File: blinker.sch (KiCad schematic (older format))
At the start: 28 parts, among them J1 TEST_1P, J2 TEST_1P, J3 TEST_1P, J4 TEST_1P, J5 TEST_1P, J6 TEST_1P, J7 TEST_1P, J8 TEST_1P, J9 TOUCH_PAD_COPPER, Q1 NTR4003NT3G, Q2 NTR4003NT3G, Q3 NTR4003NT3G, Q4 NTR4003NT3G, U1 ASMB-MTB0-0A3A2, U2 ASMB-MTB0-0A3A2, U3 ATTINY85V-10SU

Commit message: decouplign cap and pullup on reset, plus routing almost done
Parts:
- added C1: 100nf, Capacitors_SMD:C_0805_HandSoldering, symbol C
- added R11: 20K, Resistors_SMD:R_0805_HandSoldering, symbol R
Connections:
- wire segments 24 -> 31
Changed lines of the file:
@@
 	8150 5400 7800 5400
 Wire Wire Line
-	3900 3200 4650 3200
+	3900 3200 4600 3200
 Wire Wire Line
-	3800 3300 4650 3300
+	4600 3200 4650 3200
 Wire Wire Line
-	3700 3400 4650 3400
+	3800 3300 4500 3300
 Wire Wire Line
-	3600 3500 4650 3500
+	4500 3300 4650 3300
 Wire Wire Line
-	3500 3600 4650 3600
+	3700 3400 4400 3400
 Wire Wire Line
-	3400 3700 4650 3700
+	4400 3400 4650 3400
+Wire Wire Line
+	3600 3500 4300 3500
+Wire Wire Line
+	4300 3500 4650 3500
+Wire Wire Line
+	3500 3600 4200 3600
+Wire Wire Line
+	4200 3600 4650 3600
+Wire Wire Line
+	3400 3700 4100 3700
+Wire Wire Line
+	4100 3700 4650 3700
 Connection ~ 4600 3200
 Connection ~ 4500 3300
@@
 	0    -1   -1   0
 $EndComp
+$Comp
+L R R11
+U 1 1 59AD0F9D
+P 3250 3700
+F 0 "R11" V 3330 3700 50  0000 C CNN
+F 1 "20K" V 3250 3700 50  0000 C CNN
+F 2 "Resistors_SMD:R_0805_HandSoldering" V 3180 3700 50  0001 C CNN
+F 3 "" H 3250 3700 50  0001 C CNN
+	1    3250 3700
+	0    1    1    0
+$EndComp
+$Comp
+L VCC #PWR016
+U 1 1 59AD13E7
+P 3100 3700
+F 0 "#PWR016" H 3100 3550 50  0001 C CNN
+F 1 "VCC" H 3100 3850 50  0000 C CNN
+F 2 "" H 3100 3700 50  0001 C CNN
+F 3 "" H 3100 3700 50  0001 C CNN
+	1    3100 3700
+	1    0    0    -1
+$EndComp
+$Comp
+L C C1
+U 1 1 59AD17A0
+P 7350 3350
+F 0 "C1" H 7375 3450 50  0000 L CNN
+F 1 "100nf" H 7375 3250 50  0000 L CNN
+F 2 "Capacitors_SMD:C_0805_HandSoldering" H 7388 3200 50  0001 C CNN
+F 3 "" H 7350 3350 50  0001 C CNN
+	1    7350 3350
+	1    0    0    -1
+$EndComp
+Wire Wire Line
+	7350 3500 7350 3700
 $EndSCHEMATC

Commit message: pdc not in sync with sch, but silk almost done
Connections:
- wire segments 31 -> 25
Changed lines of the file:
@@
 	8150 5400 7800 5400
 Wire Wire Line
-	3900 3200 4600 3200
+	3900 3200 4650 3200
 Wire Wire Line
-	4600 3200 4650 3200
+	3800 3300 4650 3300
 Wire Wire Line
-	3800 3300 4500 3300
+	3700 3400 4650 3400
 Wire Wire Line
-	4500 3300 4650 3300
+	3600 3500 4650 3500
 Wire Wire Line
-	3700 3400 4400 3400
+	3500 3600 4650 3600
 Wire Wire Line
-	4400 3400 4650 3400
-Wire Wire Line
-	3600 3500 4300 3500
-Wire Wire Line
-	4300 3500 4650 3500
-Wire Wire Line
-	3500 3600 4200 3600
-Wire Wire Line
-	4200 3600 4650 3600
-Wire Wire Line
-	3400 3700 4100 3700
-Wire Wire Line
-	4100 3700 4650 3700
+	3400 3700 4650 3700
 Connection ~ 4600 3200
 Connection ~ 4500 3300

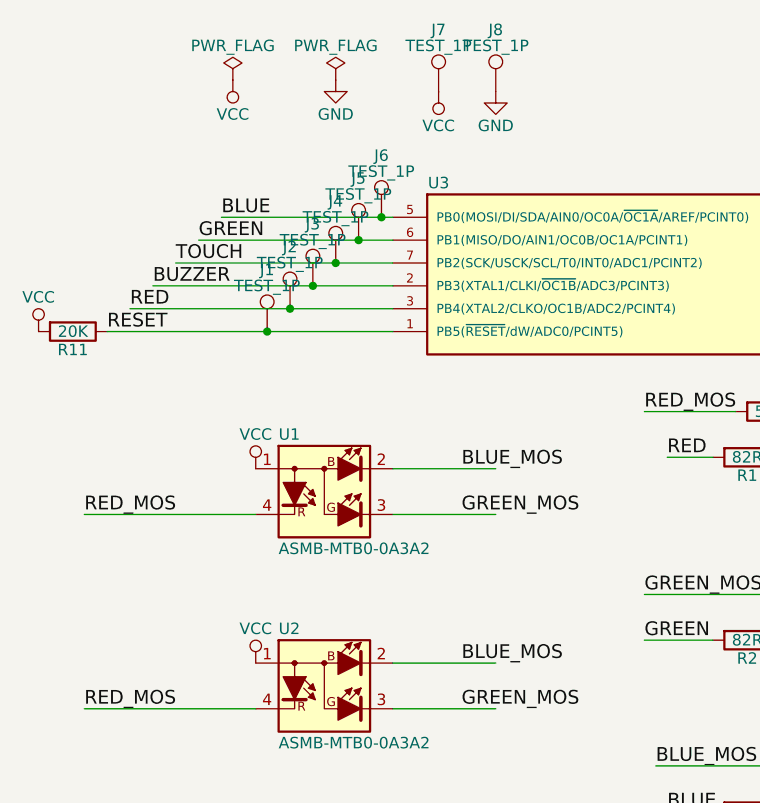
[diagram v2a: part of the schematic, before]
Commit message: assembld board, basic funcs tested. now working on version 0.2
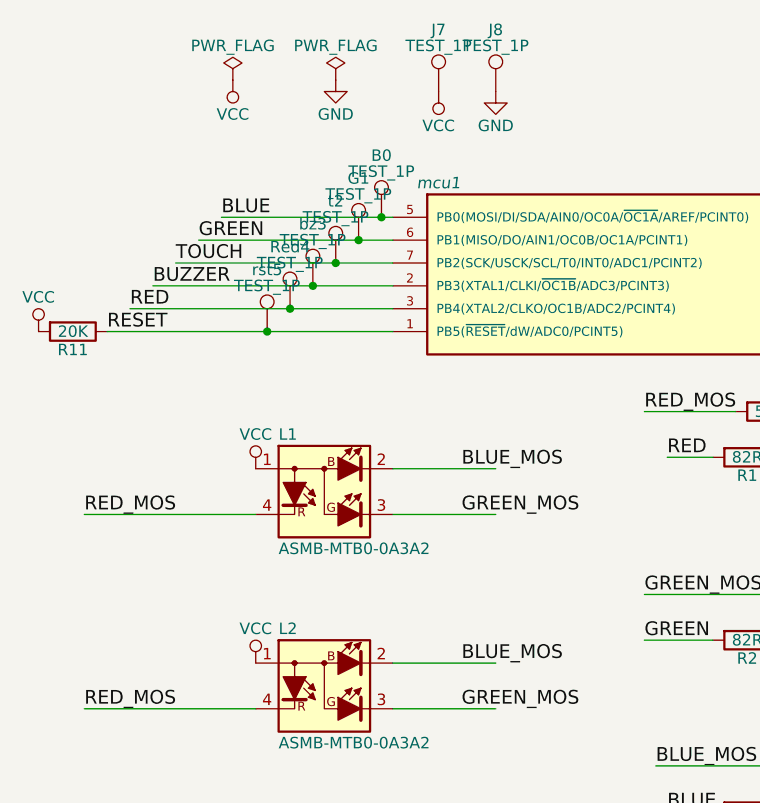
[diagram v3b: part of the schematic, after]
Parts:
- renumbered J6 to B0, J5 to G1, U1 to L1, U2 to L2, J2 to Red4, J3 to bz3, U3 to mcu1, J1 to rst5, J4 to t2
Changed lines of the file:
@@
 $EndDescr
 $Comp
-L ATTINY85-20SU U3
+L ATTINY85-20SU mcu1
 U 1 1 5991F83A
 P 6000 3450
-F 0 "U3" H 4850 3850 50  0000 C CNN
+F 0 "mcu1" H 4850 3850 50  0000 C CIN
 F 1 "ATTINY85V-10SU" H 7000 3050 50  0000 C CNN
 F 2 "Housings_SOIC:SOIC-8_3.9x4.9mm_Pitch1.27mm" H 6950 3450 50  0001 C CIN
@@
 $EndComp
 $Comp
-L ASMB-MTB0-0A3A2 U1
+L ASMB-MTB0-0A3A2 L1
 U 1 1 5993FA5E
 P 4350 4400
-F 0 "U1" H 4150 4650 50  0000 L CNN
+F 0 "L1" H 4150 4650 50  0000 L CNN
 F 1 "ASMB-MTB0-0A3A2" H 4150 4150 50  0000 L CNN
 F 2 "ASMB-MTB0-0A3A2:ASMB-MTB0-0A3A2" H 4720 4410 50  0001 L CNN
@@
 $EndComp
 $Comp
-L ASMB-MTB0-0A3A2 U2
+L ASMB-MTB0-0A3A2 L2
 U 1 1 5993FCE9
 P 4350 5250
-F 0 "U2" H 4150 5500 50  0000 L CNN
+F 0 "L2" H 4150 5500 50  0000 L CNN
 F 1 "ASMB-MTB0-0A3A2" H 4150 5000 50  0000 L CNN
 F 2 "ASMB-MTB0-0A3A2:ASMB-MTB0-0A3A2" H 4720 5260 50  0001 L CNN
@@
 $EndComp
 $Comp
-L TEST_1P J6
+L TEST_1P B0
 U 1 1 59983116
 P 4600 3200
-F 0 "J6" H 4600 3470 50  0000 C CNN
+F 0 "B0" H 4600 3470 50  0000 C CNN
 F 1 "TEST_1P" H 4600 3400 50  0000 C CNN
 F 2 "Wire_Pads:SolderWirePad_single_0-8mmDrill" H 4800 3200 50  0001 C CNN
@@
 $EndComp
 $Comp
-L TEST_1P J5
+L TEST_1P G1
 U 1 1 59983349
 P 4500 3300
-F 0 "J5" H 4500 3570 50  0000 C CNN
+F 0 "G1" H 4500 3570 50  0000 C CNN
 F 1 "TEST_1P" H 4500 3500 50  0000 C CNN
 F 2 "Wire_Pads:SolderWirePad_single_0-8mmDrill" H 4700 3300 50  0001 C CNN
@@
 $EndComp
 $Comp
-L TEST_1P J4
+L TEST_1P t2
 U 1 1 5998339F
 P 4400 3400
-F 0 "J4" H 4400 3670 50  0000 C CNN
+F 0 "t2" H 4400 3670 50  0000 C CNN
 F 1 "TEST_1P" H 4400 3600 50  0000 C CNN
 F 2 "Wire_Pads:SolderWirePad_single_0-8mmDrill" H 4600 3400 50  0001 C CNN
@@
 $EndComp
 $Comp
-L TEST_1P J3
+L TEST_1P bz3
 U 1 1 599833F8
 P 4300 3500
-F 0 "J3" H 4300 3770 50  0000 C CNN
+F 0 "bz3" H 4300 3770 50  0000 C CNN
 F 1 "TEST_1P" H 4300 3700 50  0000 C CNN
 F 2 "Wire_Pads:SolderWirePad_single_0-8mmDrill" H 4500 3500 50  0001 C CNN
@@
 $EndComp
 $Comp
-L TEST_1P J2
+L TEST_1P Red4
 U 1 1 599835BC
 P 4200 3600
-F 0 "J2" H 4200 3870 50  0000 C CNN
+F 0 "Red4" H 4200 3870 50  0000 C CNN
 F 1 "TEST_1P" H 4200 3800 50  0000 C CNN
 F 2 "Wire_Pads:SolderWirePad_single_0-8mmDrill" H 4400 3600 50  0001 C CNN
@@
 $EndComp
 $Comp
-L TEST_1P J1
+L TEST_1P rst5
 U 1 1 5998361B
 P 4100 3700
-F 0 "J1" H 4100 3970 50  0000 C CNN
+F 0 "rst5" H 4100 3970 50  0000 C CNN
 F 1 "TEST_1P" H 4100 3900 50  0000 C CNN
 F 2 "Wire_Pads:SolderWirePad_single_0-8mmDrill" H 4300 3700 50  0001 C CNN

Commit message: 2 version, already built, ready to be tested
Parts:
- added Gnd2, Vcc2: TEST_1P, wrirepad:singlesolderpad, symbol TEST_1P
- B0, G1, Red4, bz3, rst5, t2: footprint Wire_Pads:SolderWirePad_single_0-8mmDrill -> Wire_Pads:SolderWirePad_single_1-2mmDrill
- C1: footprint Capacitors_SMD:C_0805_HandSoldering -> Capacitors_SMD:C_0805
- Gnd1: renamed from J8; footprint Wire_Pads:SolderWirePad_single_0-8mmDrill -> Wire_Pads:SolderWirePad_single_1-2mmDrill
- Q1, Q2, Q3, Q4: footprint TO_SOT_Packages_SMD:SOT-23_Handsoldering -> TO_SOT_Packages_SMD:SOT-23
- R1, R11, R2, R3, R7, R8: footprint Resistors_SMD:R_0805_HandSoldering -> Resistors_SMD:R_0805
- R10: value 27R -> 33R; footprint Resistors_SMD:R_0805_HandSoldering -> Resistors_SMD:R_0805
- R4: value 50R -> 33R; footprint Resistors_SMD:R_0805_HandSoldering -> Resistors_SMD:R_0805
- R5, R6: value 34R -> 33R; footprint Resistors_SMD:R_0805_HandSoldering -> Resistors_SMD:R_0805
- R9: value 10K -> 20K; footprint Resistors_SMD:R_0805_HandSoldering -> Resistors_SMD:R_0805
- Vcc1: renamed from J7; footprint Wire_Pads:SolderWirePad_single_0-8mmDrill -> Wire_Pads:SolderWirePad_single_1-2mmDrill
- mcu1: footprint Housings_SOIC:SOIC-8_3.9x4.9mm_Pitch1.27mm -> Housings_SOIC:SOIJ-8_5.3x5.3mm_Pitch1.27mm
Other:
- note added: "testare quale valore nel range 1kOhm 100kOhm è più appropriato"
- moved on the sheet: Gnd1, Vcc1
